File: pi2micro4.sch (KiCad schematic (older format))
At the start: 17 parts, among them M1 microduino_base, M2 microduino_base, M3 microduino_base, M4 microduino_base, P1 CONN_13X2, U1 NCP1117ST33T3G, U2 txs0104e

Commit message: nuevo buffer
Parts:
- added K1, K2: CONN_3, SIL-3, symbol CONN_3
- added R3, R4, R5, R6: 1k, SMD-0603, symbol R
- added U3: txs0104e, TSSOP-14, symbol txs0104e
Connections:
- net +5V: now also U3.1 (VCCA)
- net 3V3_RB: now also K1.1 (P1), K2.1 (P1), R5.1, U3.14 (VCCB)
- net A4: now also U2.4 (A3)
- net A5: now also U2.5 (A4)
- net D11: now also U3.3 (A2)
- net D12: now also U3.4 (A3)
- net D13: now also U3.5 (A4)
- net D2: no longer U2.5 (A4)
- net GND: now also K1.3 (P3), K2.3 (P3), R3.2, R4.2, U3.7 (GND)
- net RST: now also U3.2 (A1); no longer U2.4 (A3)
- net Rp_GPIO: no longer U2.10 (B4)
- net Rp_RST: now also U3.13 (B1); no longer U2.11 (B3)
- net Rp_MOSI: now reaches P1.19 (P19)
- net Rp_MOSI: now also U3.12 (B2)
- net Rp_MISO: now reaches P1.21 (P21)
- net Rp_MISO: now also U3.11 (B3)
- net Rp_SCLK: now reaches P1.23 (P23)
- net Rp_SCLK: now also U3.10 (B4)
- net Rp_SDA: now reaches P1.3 (P3)
- net Rp_SDA: now also U2.11 (B3), R5.2
- net Rp_SCL: now reaches P1.5 (P5)
- net Rp_SCL: now also U2.10 (B4), R6.2
- net at U2.8 (OE): now also K2.2 (PM), R4.1
- new net: K1.2 (PM), R3.1, U3.8 (OE)
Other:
- moved on the sheet: C5, C6, M3, M4, P1, U2

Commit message: corregido el footprint del microduino
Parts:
- added R7: 1k, SMD-0603, symbol R
- added SW1: SW_PUSH, SW_PUSH_SMALL, symbol SW_PUSH
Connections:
- net +5V: now also R7.1
- net GND: now also SW1.1
- net RST: now also R7.2, SW1.2
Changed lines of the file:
@@
 $EndComp
 $Comp
-L GND #PWR3
+L GND #PWR01
 U 1 1 53FD4A2D
 P 900 1700
-F 0 "#PWR3" H 900 1700 30  0001 C CNN
+F 0 "#PWR01" H 900 1700 30  0001 C CNN
 F 1 "GND" H 900 1630 30  0001 C CNN
 F 2 "" H 900 1700 60  0000 C CNN
@@
 $EndComp
 $Comp
-L +5V #PWR4
+L +5V #PWR02
 U 1 1 53FD4A41
 P 900 3200
-F 0 "#PWR4" H 900 3290 20  0001 C CNN
+F 0 "#PWR02" H 900 3290 20  0001 C CNN
 F 1 "+5V" H 900 3290 30  0000 C CNN
 F 2 "" H 900 3200 60  0000 C CNN
@@
 A7
 $Comp
-L +3.3V #PWR1
+L +3.3V #PWR03
 U 1 1 53FD4B20
 P 750 3200
-F 0 "#PWR1" H 750 3160 30  0001 C CNN
+F 0 "#PWR03" H 750 3160 30  0001 C CNN
 F 1 "+3.3V" H 750 3310 30  0000 C CNN
 F 2 "" H 750 3200 60  0000 C CNN
@@
 $EndComp
 $Comp
-L GND #PWR9
+L GND #PWR04
 U 1 1 53FD4C14
 P 3200 1700
-F 0 "#PWR9" H 3200 1700 30  0001 C CNN
+F 0 "#PWR04" H 3200 1700 30  0001 C CNN
 F 1 "GND" H 3200 1630 30  0001 C CNN
 F 2 "" H 3200 1700 60  0000 C CNN
@@
 $EndComp
 $Comp
-L +5V #PWR10
+L +5V #PWR05
 U 1 1 53FD4C1A
 P 3200 3200
-F 0 "#PWR10" H 3200 3290 20  0001 C CNN
+F 0 "#PWR05" H 3200 3290 20  0001 C CNN
 F 1 "+5V" H 3200 3290 30  0000 C CNN
 F 2 "" H 3200 3200 60  0000 C CNN
@@
 A7
 $Comp
-L +3.3V #PWR7
+L +3.3V #PWR06
 U 1 1 53FD4C53
 P 3050 3200
-F 0 "#PWR7" H 3050 3160 30  0001 C CNN
+F 0 "#PWR06" H 3050 3160 30  0001 C CNN
 F 1 "+3.3V" H 3050 3310 30  0000 C CNN
 F 2 "" H 3050 3200 60  0000 C CNN
@@
 $EndComp
 $Comp
-L GND #PWR5
+L GND #PWR07
 U 1 1 53FD4C65
 P 900 4400
-F 0 "#PWR5" H 900 4400 30  0001 C CNN
+F 0 "#PWR07" H 900 4400 30  0001 C CNN
 F 1 "GND" H 900 4330 30  0001 C CNN
 F 2 "" H 900 4400 60  0000 C CNN
@@
 $EndComp
 $Comp
-L +5V #PWR6
+L +5V #PWR08
 U 1 1 53FD4C6B
 P 900 5900
-F 0 "#PWR6" H 900 5990 20  0001 C CNN
+F 0 "#PWR08" H 900 5990 20  0001 C CNN
 F 1 "+5V" H 900 5990 30  0000 C CNN
 F 2 "" H 900 5900 60  0000 C CNN
@@
 A7
 $Comp
-L +3.3V #PWR2
+L +3.3V #PWR09
 U 1 1 53FD4CA4
 P 750 5900
-F 0 "#PWR2" H 750 5860 30  0001 C CNN
+F 0 "#PWR09" H 750 5860 30  0001 C CNN
 F 1 "+3.3V" H 750 6010 30  0000 C CNN
 F 2 "" H 750 5900 60  0000 C CNN
@@
 $EndComp
 $Comp
-L GND #PWR11
+L GND #PWR010
 U 1 1 53FD4CB6
 P 3200 4400
-F 0 "#PWR11" H 3200 4400 30  0001 C CNN
+F 0 "#PWR010" H 3200 4400 30  0001 C CNN
 F 1 "GND" H 3200 4330 30  0001 C CNN
 F 2 "" H 3200 4400 60  0000 C CNN
@@
 $EndComp
 $Comp
-L +5V #PWR12
+L +5V #PWR011
 U 1 1 53FD4CBC
 P 3200 5900
-F 0 "#PWR12" H 3200 5990 20  0001 C CNN
+F 0 "#PWR011" H 3200 5990 20  0001 C CNN
 F 1 "+5V" H 3200 5990 30  0000 C CNN
 F 2 "" H 3200 5900 60  0000 C CNN
@@
 A7
 $Comp
-L +3.3V #PWR8
+L +3.3V #PWR012
 U 1 1 53FD4CF5
 P 3050 5900
-F 0 "#PWR8" H 3050 5860 30  0001 C CNN
+F 0 "#PWR012" H 3050 5860 30  0001 C CNN
 F 1 "+3.3V" H 3050 6010 30  0000 C CNN
 F 2 "" H 3050 5900 60  0000 C CNN
@@
 $EndComp
 $Comp
-L +5V #PWR29
+L +5V #PWR013
 U 1 1 53FFB226
 P 10450 2400
-F 0 "#PWR29" H 10450 2490 20  0001 C CNN
+F 0 "#PWR013" H 10450 2490 20  0001 C CNN
 F 1 "+5V" H 10450 2490 30  0000 C CNN
 F 2 "" H 10450 2400 60  0000 C CNN
@@
 Connection ~ 10450 2450
 $Comp
-L GND #PWR30
+L GND #PWR014
 U 1 1 53FFB44F
 P 10500 3100
-F 0 "#PWR30" H 10500 3100 30  0001 C CNN
+F 0 "#PWR014" H 10500 3100 30  0001 C CNN
 F 1 "GND" H 10500 3030 30  0001 C CNN
 F 2 "" H 10500 3100 60  0000 C CNN
@@
 $EndComp
 $Comp
-L GND #PWR34
+L GND #PWR015
 U 1 1 53FFB456
 P 10900 2850
-F 0 "#PWR34" H 10900 2850 30  0001 C CNN
+F 0 "#PWR015" H 10900 2850 30  0001 C CNN
 F 1 "GND" H 10900 2780 30  0001 C CNN
 F 2 "" H 10900 2850 60  0000 C CNN
@@
 $EndComp
 $Comp
-L GND #PWR31
+L GND #PWR016
 U 1 1 53FFB45C
 P 10500 3400
-F 0 "#PWR31" H 10500 3400 30  0001 C CNN
+F 0 "#PWR016" H 10500 3400 30  0001 C CNN
 F 1 "GND" H 10500 3330 30  0001 C CNN
 F 2 "" H 10500 3400 60  0000 C CNN
@@
 $EndComp
 $Comp
-L GND #PWR24
+L GND #PWR017
 U 1 1 53FFB462
 P 9400 3700
-F 0 "#PWR24" H 9400 3700 30  0001 C CNN
+F 0 "#PWR017" H 9400 3700 30  0001 C CNN
 F 1 "GND" H 9400 3630 30  0001 C CNN
 F 2 "" H 9400 3700 60  0000 C CNN
@@
 $EndComp
 $Comp
-L GND #PWR22
+L GND #PWR018
 U 1 1 53FFB468
 P 9050 3000
-F 0 "#PWR22" H 9050 3000 30  0001 C CNN
+F 0 "#PWR018" H 9050 3000 30  0001 C CNN
 F 1 "GND" H 9050 2930 30  0001 C CNN
 F 2 "" H 9050 3000 60  0000 C CNN
@@
 $EndComp
 $Comp
-L +5V #PWR36
+L +5V #PWR019
 U 1 1 5400DF7F
 P 11050 550
-F 0 "#PWR36" H 11050 640 20  0001 C CNN
+F 0 "#PWR019" H 11050 640 20  0001 C CNN
 F 1 "+5V" H 11050 640 30  0000 C CNN
 F 2 "" H 11050 550 60  0000 C CNN
@@
 $EndComp
 $Comp
-L GND #PWR35
+L GND #PWR020
 U 1 1 5400DFEC
 P 10950 1750
-F 0 "#PWR35" H 10950 1750 30  0001 C CNN
+F 0 "#PWR020" H 10950 1750 30  0001 C CNN
 F 1 "GND" H 10950 1680 30  0001 C CNN
 F 2 "" H 10950 1750 60  0000 C CNN
@@
 $EndComp
 $Comp
-L +3.3V #PWR33
+L +3.3V #PWR021
 U 1 1 5400DFFE
 P 10850 550
-F 0 "#PWR33" H 10850 510 30  0001 C CNN
+F 0 "#PWR021" H 10850 510 30  0001 C CNN
 F 1 "+3.3V" H 10850 660 30  0000 C CNN
 F 2 "" H 10850 550 60  0000 C CNN
@@
 $EndComp
 $Comp
-L +3.3V #PWR25
+L +3.3V #PWR022
 U 1 1 5400E522
 P 9650 1150
-F 0 "#PWR25" H 9650 1110 30  0001 C CNN
+F 0 "#PWR022" H 9650 1110 30  0001 C CNN
 F 1 "+3.3V" H 9650 1260 30  0000 C CNN
 F 2 "" H 9650 1150 60  0000 C CNN
@@
 $EndComp
 $Comp
-L GND #PWR23
+L GND #PWR023
 U 1 1 5400E528
 P 9150 1500
-F 0 "#PWR23" H 9150 1500 30  0001 C CNN
+F 0 "#PWR023" H 9150 1500 30  0001 C CNN
 F 1 "GND" H 9150 1430 30  0001 C CNN
 F 2 "" H 9150 1500 60  0000 C CNN
@@
 	9150 1450 9150 1500
 $Comp
-L +5V #PWR21
+L +5V #PWR024
 U 1 1 5400E5CC
 P 8700 1100
-F 0 "#PWR21" H 8700 1190 20  0001 C CNN
+F 0 "#PWR024" H 8700 1190 20  0001 C CNN
 F 1 "+5V" H 8700 1190 30  0000 C CNN
 F 2 "" H 8700 1100 60  0000 C CNN
@@
 $EndComp
 $Comp
-L +3.3V #PWR26
+L +3.3V #PWR025
 U 1 1 5400E778
 P 10100 950
-F 0 "#PWR26" H 10100 910 30  0001 C CNN
+F 0 "#PWR025" H 10100 910 30  0001 C CNN
 F 1 "+3.3V" H 10100 1060 30  0000 C CNN
 F 2 "" H 10100 950 60  0000 C CNN
@@
 $EndComp
 $Comp
-L GND #PWR27
+L GND #PWR026
 U 1 1 5400E77E
 P 10100 1500
-F 0 "#PWR27" H 10100 1500 30  0001 C CNN
+F 0 "#PWR026" H 10100 1500 30  0001 C CNN
 F 1 "GND" H 10100 1430 30  0001 C CNN
 F 2 "" H 10100 1500 60  0000 C CNN
@@
 $EndComp
 $Comp
-L GND #PWR20
+L GND #PWR027
 U 1 1 5400EB82
 P 8000 1450
-F 0 "#PWR20" H 8000 1450 30  0001 C CNN
+F 0 "#PWR027" H 8000 1450 30  0001 C CNN
 F 1 "GND" H 8000 1380 30  0001 C CNN
 F 2 "" H 8000 1450 60  0000 C CNN
@@
 	8350 900  8000 900
 $Comp
-L +5V #PWR19
+L +5V #PWR028
 U 1 1 5400EB8F
 P 8000 850
-F 0 "#PWR19" H 8000 940 20  0001 C CNN
+F 0 "#PWR028" H 8000 940 20  0001 C CNN
 F 1 "+5V" H 8000 940 30  0000 C CNN
 F 2 "" H 8000 850 60  0000 C CNN
@@
 $EndComp
 $Comp
-L GND #PWR15
+L GND #PWR029
 U 1 1 5400F690
 P 6250 3150
-F 0 "#PWR15" H 6250 3150 30  0001 C CNN
+F 0 "#PWR029" H 6250 3150 30  0001 C CNN
 F 1 "GND" H 6250 3080 30  0001 C CNN
 F 2 "" H 6250 3150 60  0000 C CNN
@@
 	10650 4800 10650 4650
 $Comp
-L GND #PWR32
+L GND #PWR030
 U 1 1 5400F75B
 P 10500 4900
-F 0 "#PWR32" H 10500 4900 30  0001 C CNN
+F 0 "#PWR030" H 10500 4900 30  0001 C CNN
 F 1 "GND" H 10500 4830 30  0001 C CNN
 F 2 "" H 10500 4900 60  0000 C CNN
@@
 $EndComp
 $Comp
-L +5V #PWR16
+L +5V #PWR031
 U 1 1 5400F77E
 P 6300 2450
-F 0 "#PWR16" H 6300 2540 20  0001 C CNN
+F 0 "#PWR031" H 6300 2540 20  0001 C CNN
 F 1 "+5V" H 6300 2540 30  0000 C CNN
 F 2 "" H 6300 2450 60  0000 C CNN
@@
 $EndComp
 $Comp
-L +5V #PWR28
+L +5V #PWR032
 U 1 1 5400F78B
 P 10350 4150
-F 0 "#PWR28" H 10350 4240 20  0001 C CNN
+F 0 "#PWR032" H 10350 4240 20  0001 C CNN
 F 1 "+5V" H 10350 4240 30  0000 C CNN
 F 2 "" H 10350 4150 60  0000 C CNN
@@
 $EndComp
 $Comp
-L GND #PWR13
+L GND #PWR033
 U 1 1 540A2804
 P 6150 5250
-F 0 "#PWR13" H 6150 5250 30  0001 C CNN
+F 0 "#PWR033" H 6150 5250 30  0001 C CNN
 F 1 "GND" H 6150 5180 30  0001 C CNN
 F 2 "" H 6150 5250 60  0000 C CNN
@@
 	6150 5200 6150 5250
 $Comp
-L +5V #PWR14
+L +5V #PWR034
 U 1 1 540A280C
 P 6200 4550
-F 0 "#PWR14" H 6200 4640 20  0001 C CNN
+F 0 "#PWR034" H 6200 4640 20  0001 C CNN
 F 1 "+5V" H 6200 4640 30  0000 C CNN
 F 2 "" H 6200 4550 60  0000 C CNN
@@
 	7750 4000 7750 4100
 $Comp
-L GND #PWR18
+L GND #PWR035
 U 1 1 540B00AB
 P 7750 4100
-F 0 "#PWR18" H 7750 4100 30  0001 C CNN
+F 0 "#PWR035" H 7750 4100 30  0001 C CNN
 F 1 "GND" H 7750 4030 30  0001 C CNN
 F 2 "" H 7750 4100 60  0000 C CNN
@@
 	7650 6100 7650 6200
 $Comp
-L GND #PWR17
+L GND #PWR036
 U 1 1 540B070B
 P 7650 6200
-F 0 "#PWR17" H 7650 6200 30  0001 C CNN
+F 0 "#PWR036" H 7650 6200 30  0001 C CNN
 F 1 "GND" H 7650 6130 30  0001 C CNN
 F 2 "" H 7650 6200 60  0000 C CNN
@@
 	1    0    0    -1
 $EndComp
+$Comp
+L SW_PUSH SW1
+U 1 1 540C9A75
+P 5800 6450
+F 0 "SW1" H 5950 6560 50  0000 C CNN
+F 1 "SW_PUSH" H 5800 6370 50  0000 C CNN
+F 2 "SW_PUSH_SMALL" H 5800 6450 60  0001 C CNN
+F 3 "" H 5800 6450 60  0000 C CNN
+	1    5800 6450
+	1    0    0    -1
+$EndComp
+$Comp
+L R R7
+U 1 1 540C9A87
+P 6200 6150
+F 0 "R7" V 6280 6150 40  0000 C CNN
+F 1 "1k" V 6207 6151 40  0000 C CNN
+F 2 "SMD-0603" V 6130 6150 30  0001 C CNN
+F 3 "" H 6200 6150 30  0000 C CNN
+	1    6200 6150
+	1    0    0    -1
+$EndComp
+$Comp
+L +5V #PWR037
+U 1 1 540C9A99
+P 6200 5800
+F 0 "#PWR037" H 6200 5890 20  0001 C CNN
+F 1 "+5V" H 6200 5890 30  0000 C CNN
+F 2 "" H 6200 5800 60  0000 C CNN
+F 3 "" H 6200 5800 60  0000 C CNN
+	1    6200 5800
+	1    0    0    -1
+$EndComp
+Wire Wire Line
+	6200 5800 6200 5900
+Wire Wire Line
+	6100 6450 6450 6450
+Text Label 6450 6450 2    60   ~ 0
+RST
+Wire Wire Line
+	5500 6450 5500 6550
+$Comp
+L GND #PWR038
+U 1 1 540C9B81
+P 5500 6550
+F 0 "#PWR038" H 5500 6550 30  0001 C CNN
+F 1 "GND" H 5500 6480 30  0001 C CNN
+F 2 "" H 5500 6550 60  0000 C CNN
+F 3 "" H 5500 6550 60  0000 C CNN
+	1    5500 6550
+	1    0    0    -1
+$EndComp
+Wire Wire Line
+	6200 6400 6200 6450
+Connection ~ 6200 6450
 $EndSCHEMATC

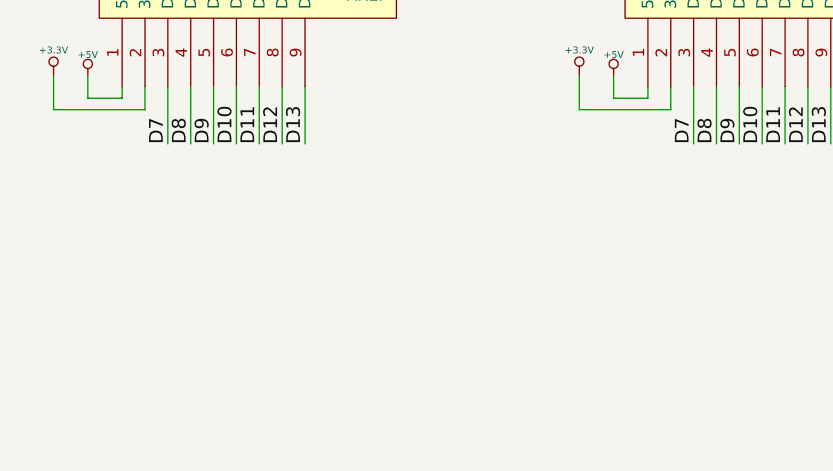
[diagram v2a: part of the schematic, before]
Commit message: 6 conectores para servos
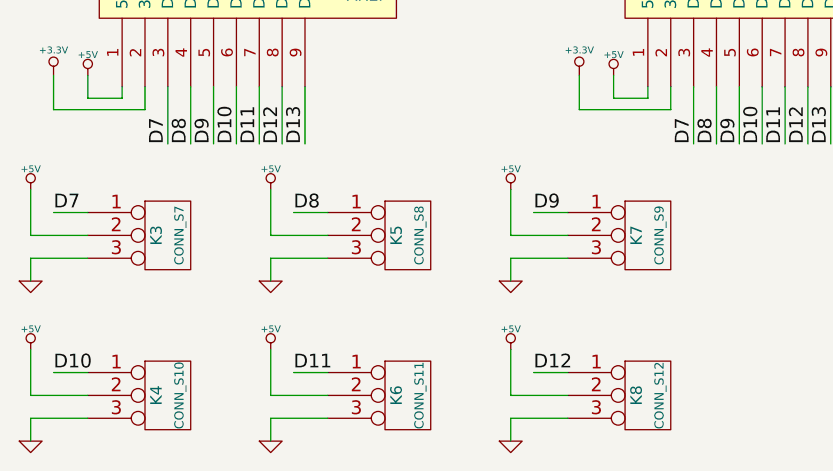
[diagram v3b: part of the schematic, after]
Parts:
- added K3: CONN_S7, SIL-3, symbol CONN_3
- added K4: CONN_S10, SIL-3, symbol CONN_3
- added K5: CONN_S8, SIL-3, symbol CONN_3
- added K6: CONN_S11, SIL-3, symbol CONN_3
- added K7: CONN_S9, SIL-3, symbol CONN_3
- added K8: CONN_S12, SIL-3, symbol CONN_3
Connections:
- net +5V: now also K3.2 (PM), K4.2 (PM), K5.2 (PM), K6.2 (PM), K7.2 (PM), K8.2 (PM)
- net D10: now also K4.1 (P1)
- net D11: now also K6.1 (P1)
- net D12: now also K8.1 (P1)
- net D7: now also K3.1 (P1)
- net D8: now also K5.1 (P1)
- net D9: now also K7.1 (P1)
- net GND: now also K3.3 (P3), K4.3 (P3), K5.3 (P3), K6.3 (P3), K7.3 (P3), K8.3 (P3)

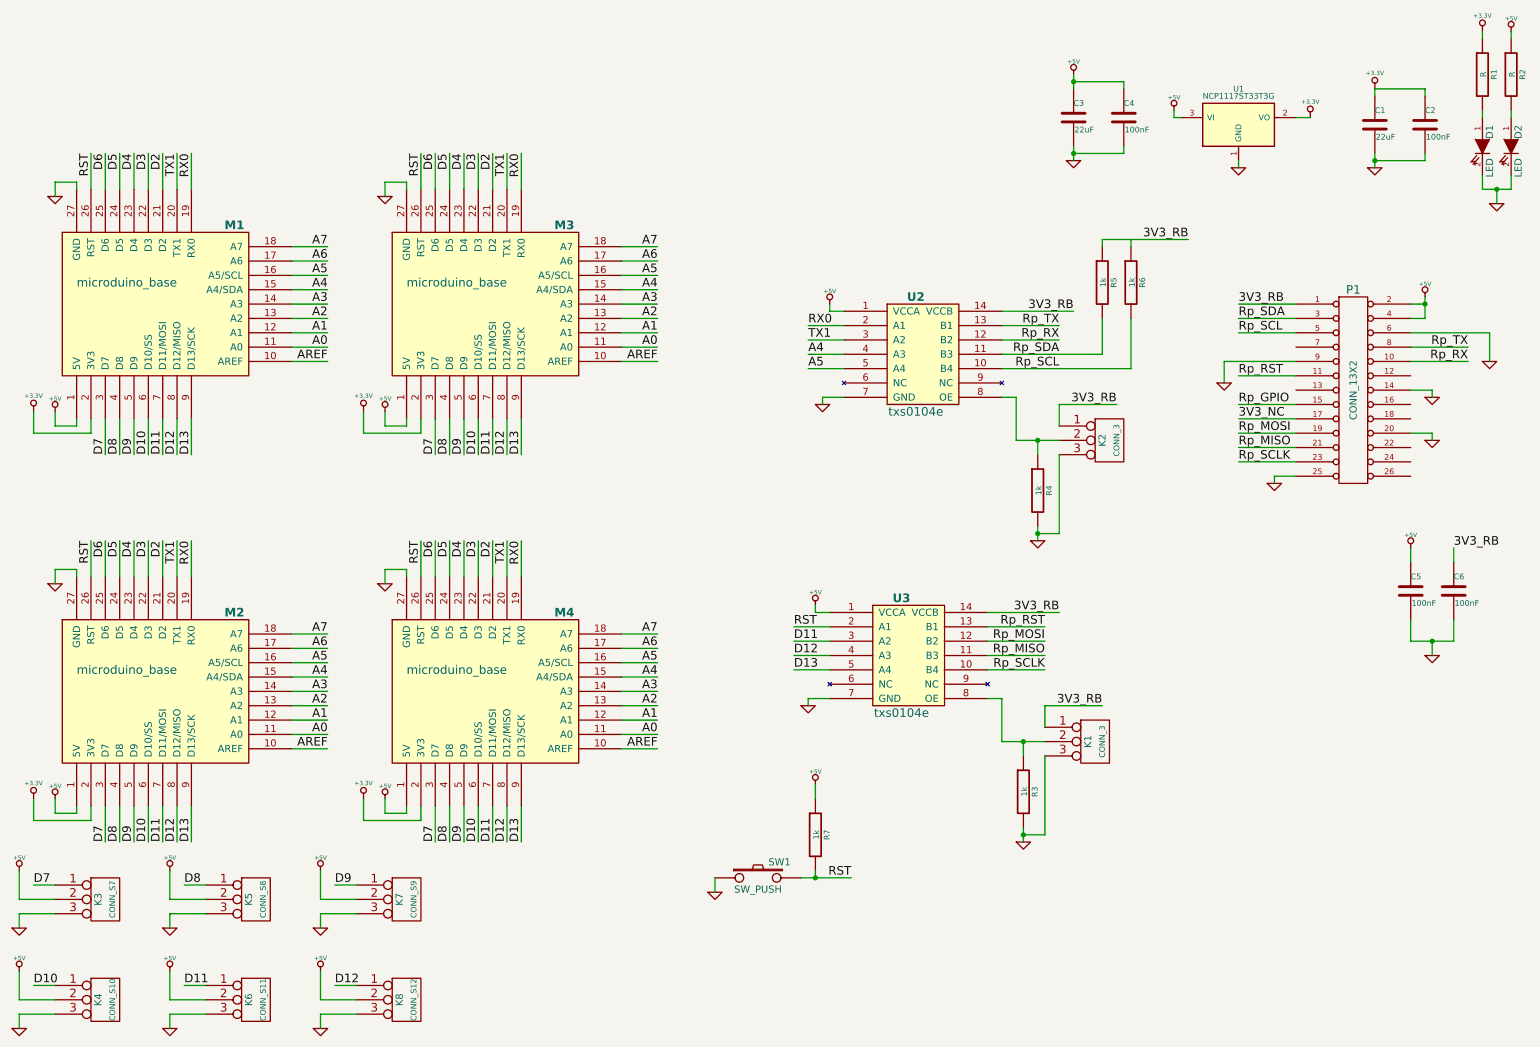
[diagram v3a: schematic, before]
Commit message: conectores de entrada analoga y uart a las raspberry pi
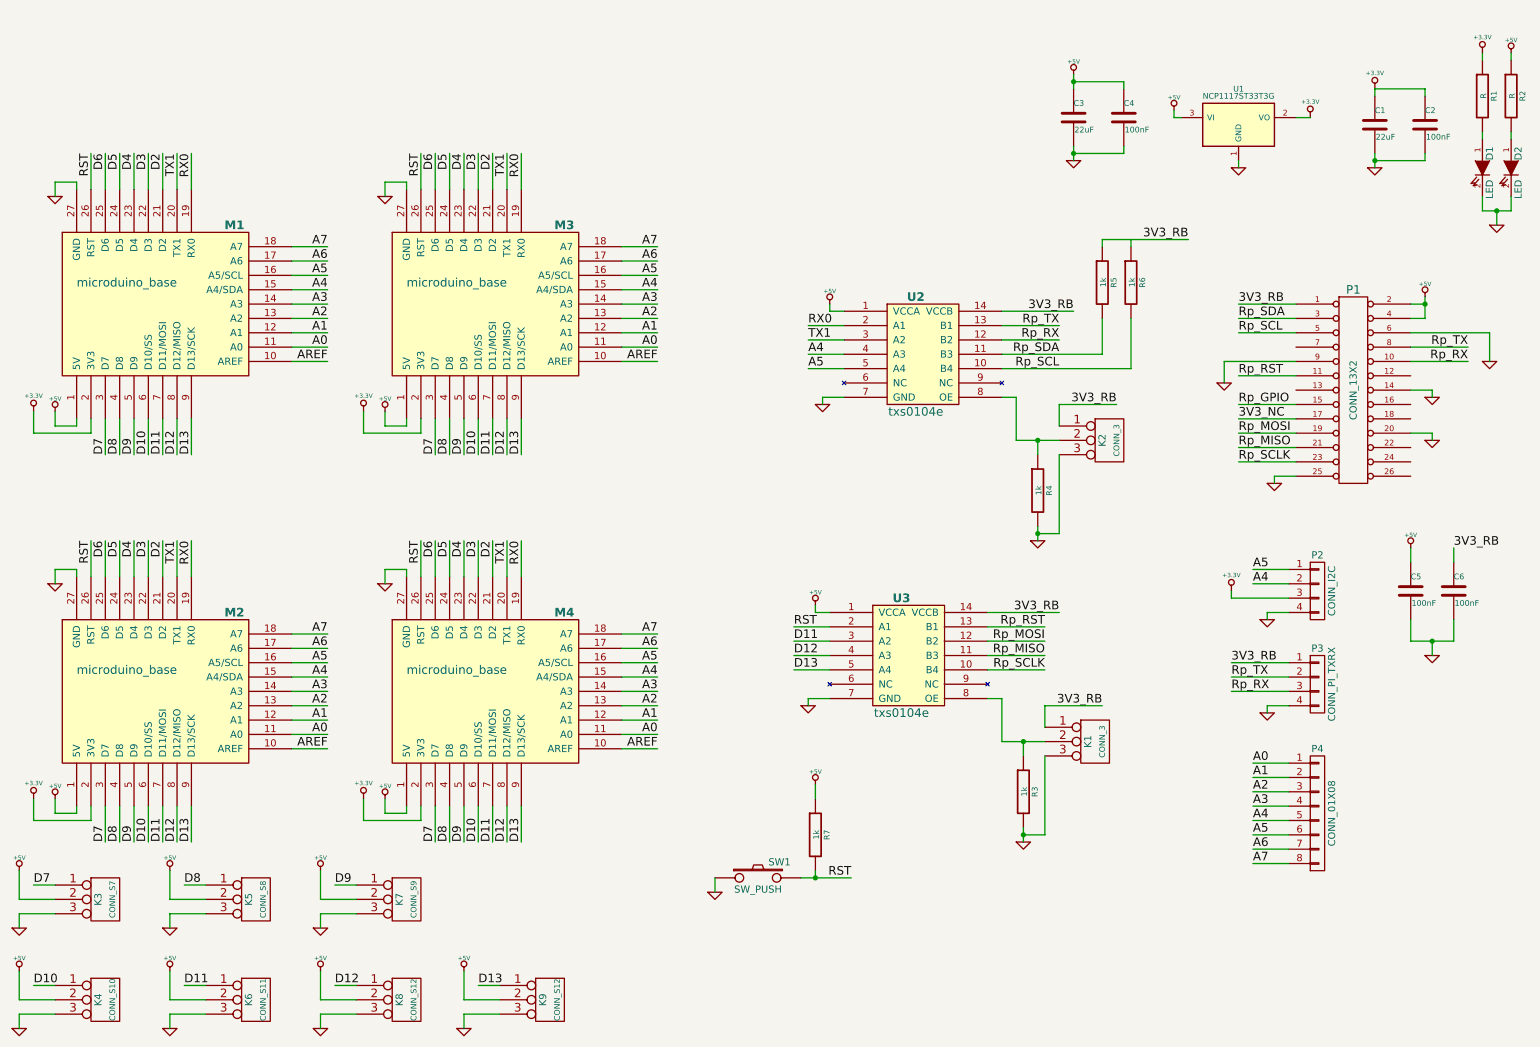
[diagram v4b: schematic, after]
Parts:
- added K9: CONN_S12, SIL-3, symbol CONN_3
- added P2: CONN_I2C, SIL-4, symbol CONN_01X04
- added P3: CONN_PI_TXRX, SIL-4, symbol CONN_01X04
- added P4: CONN_01X08, symbol CONN_01X08
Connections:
- net +3.3V: now also P2.3 (P3)
- net +5V: now also K9.2 (PM)
- net 3V3_RB: now also P3.1 (P1)
- net A0: now also P4.1 (P1)
- net A1: now also P4.2 (P2)
- net A2: now also P4.3 (P3)
- net A3: now also P4.4 (P4)
- net A4: now also P2.2 (P2), P4.5 (P5)
- net A5: now also P2.1 (P1), P4.6 (P6)
- net A6: now also P4.7 (P7)
- net A7: now also P4.8 (P8)
- net D13: now also K9.1 (P1)
- net GND: now also K9.3 (P3), P2.4 (P4), P3.4 (P4)
- net Rp_RX: now also P3.3 (P3)
- net Rp_TX: now also P3.2 (P2)
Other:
- moved on the sheet: D1, D2, R1, R2

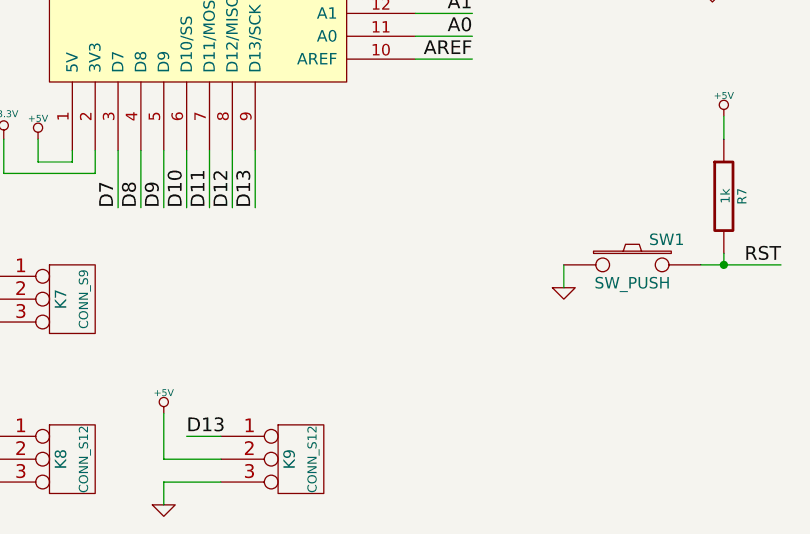
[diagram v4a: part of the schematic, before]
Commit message: D13 led
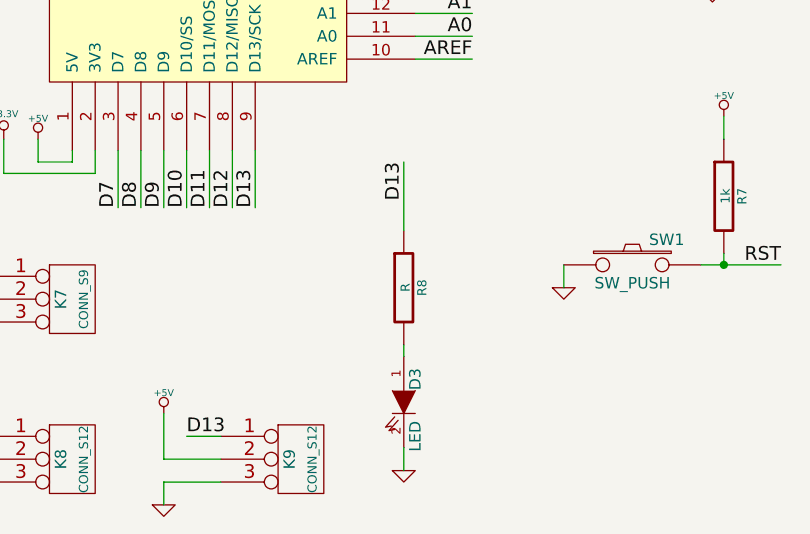
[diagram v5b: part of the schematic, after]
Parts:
- added D3: LED, SMD-0603, symbol LED
- added R8: R, SMD-0603, symbol R
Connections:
- net D13: now also R8.1
- net GND: now also D3.2 (K)
- new net: D3.1 (A), R8.2
